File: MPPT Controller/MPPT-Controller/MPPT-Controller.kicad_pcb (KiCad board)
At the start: 4 copper layers, 81 parts, among them J1 Conn_01x02_Pin, J2 Conn_01x02_Pin, J3 Conn_01x02_Pin, J4 Conn_01x02_Pin, J5 USB_C_Receptacle_USB2.0_16P, J6 Conn_01x02_Pin, M1 Fan_4pin, Q1 IRL540N, SW1 SW_SPDT, U1 ADS1115IDGS, U2 ESP32-WROOM-32D, U3 CH340C, U4 LM1117DT-3.3, U5 LM2596S-ADJ, U6 TC4422, U7 ADS1115IDGS

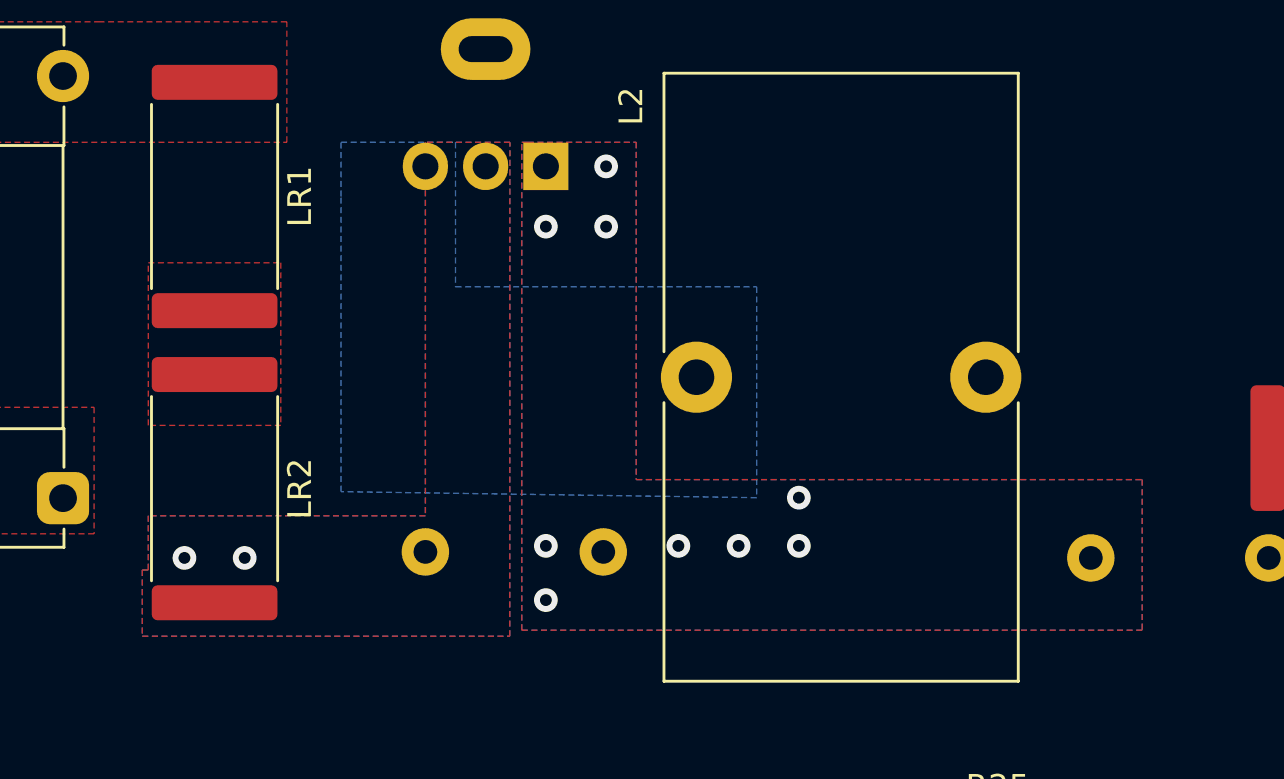
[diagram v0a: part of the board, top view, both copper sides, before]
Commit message: Single Layer
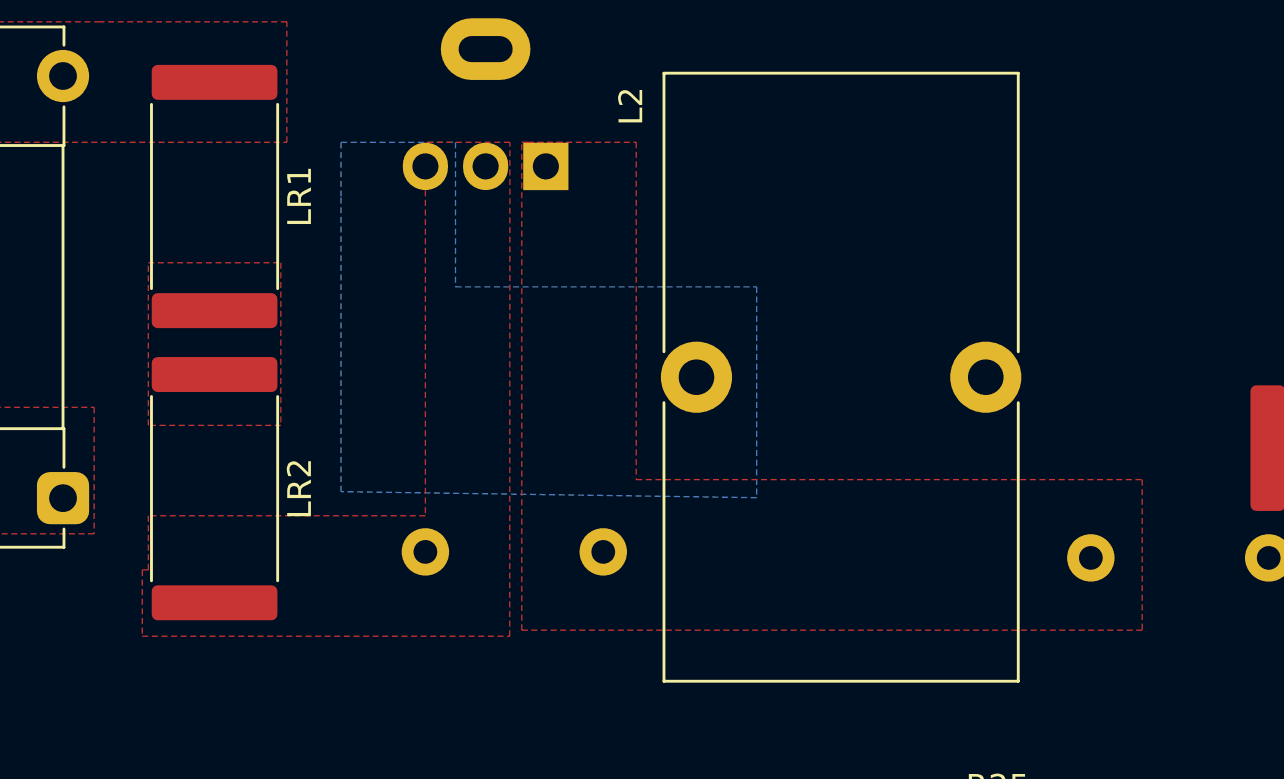
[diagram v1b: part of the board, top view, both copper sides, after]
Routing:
- net VinterA: vias 2 -> 0
- net Net-(D10-A): vias 9 -> 0
- removed copper zone on B.Cu, net Net-(D10-A)
- removed copper zone on B.Cu, net VinterA
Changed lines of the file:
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@@
 		)
 		(property "Value" "470u"
-			(at 3.25 -2 -180)
+			(at 3.25 -2 180)
 			(layer "F.Fab")
 			(effects
@@
 	)
 	(via
-		(at 58.42 121.92)
-		(size 1)
-		(drill 0.5)
-		(layers "F.Cu" "B.Cu")
-		(free yes)
-		(net 4)
-	)
-	(via
-		(at 55.88 121.92)
-		(size 1)
-		(drill 0.5)
-		(layers "F.Cu" "B.Cu")
-		(free yes)
-		(net 4)
-	)
-	(via
 		(at 144 50.5)
 		(size 1)
@@
 		(layers "F.Cu" "B.Cu")
 		(net 13)
-	)
-	(via
-		(at 71.12 107.95)
-		(size 1)
-		(drill 0.5)
-		(layers "F.Cu" "B.Cu")
-		(free yes)
-		(net 15)
-	)
-	(via
-		(at 73.66 107.95)
-		(size 1)
-		(drill 0.5)
-		(layers "F.Cu" "B.Cu")
-		(free yes)
-		(net 15)
-	)
-	(via
-		(at 71.12 123.698)
-		(size 1)
-		(drill 0.5)
-		(layers "F.Cu" "B.Cu")
-		(free yes)
-		(net 15)
-	)
-	(via
-		(at 73.66 105.41)
-		(size 1)
-		(drill 0.5)
-		(layers "F.Cu" "B.Cu")
-		(free yes)
-		(net 15)
-	)
-	(via
-		(at 81.788 119.38)
-		(size 1)
-		(drill 0.5)
-		(layers "F.Cu" "B.Cu")
-		(free yes)
-		(net 15)
-	)
-	(via
-		(at 79.248 121.412)
-		(size 1)
-		(drill 0.5)
-		(layers "F.Cu" "B.Cu")
-		(free yes)
-		(net 15)
-	)
-	(via
-		(at 81.788 121.412)
-		(size 1)
-		(drill 0.5)
-		(layers "F.Cu" "B.Cu")
-		(free yes)
-		(net 15)
-	)
-	(via
-		(at 71.12 121.412)
-		(size 1)
-		(drill 0.5)
-		(layers "F.Cu" "B.Cu")
-		(free yes)
-		(net 15)
-	)
-	(via
-		(at 76.708 121.412)
-		(size 1)
-		(drill 0.5)
-		(layers "F.Cu" "B.Cu")
-		(free yes)
-		(net 15)
 	)
 	(zone
@@
 	)
 	(zone
+		(net 4)
+		(net_name "VinterA")
+		(layer "F.Cu")
+		(hatch edge 0.5)
+		(priority 7)
+		(connect_pads yes
+			(clearance 0.6)
+		)
+		(min_thickness 0.25)
+		(filled_areas_thickness no)
+		(fill yes
+			(thermal_gap 0)
+			(thermal_bridge_width 1)
+		)
+		(polygon
+			(pts
+				(xy 54.356 122.428) (xy 54.102 122.428) (xy 54.102 125.222) (xy 69.596306 125.222) (xy 69.604659 104.394)
+				(xy 66.04 104.394) (xy 66.04 120.142) (xy 54.356 120.142)
+			)
+		)
+	)
+	(zone
 		(net 90)
 		(net_name "Net-(J1-Pin_2)")
@@
 			(pts
 				(xy 30.48 115.57) (xy 52.07 115.57) (xy 52.07 120.904) (xy 30.48 120.904)
+			)
+		)
+	)
+	(zone
+		(net 15)
+		(net_name "Net-(D10-A)")
+		(layer "F.Cu")
+		(hatch edge 0.5)
+		(priority 8)
+		(connect_pads yes
+			(clearance 0.5)
+		)
+		(min_thickness 0.25)
+		(filled_areas_thickness no)
+		(fill yes
+			(thermal_gap 0)
+			(thermal_bridge_width 1)
+		)
+		(polygon
+			(pts
+				(xy 70.358 104.394) (xy 74.93 104.394) (xy 74.93 118.618) (xy 96.266 118.618) (xy 96.266 124.968)
+				(xy 70.104 124.968) (xy 70.104 104.394)
 			)
 		)
@@
 	)
 	(zone
-		(net 4)
-		(net_name "VinterA")
-		(layers "F.Cu" "B.Cu")
-		(hatch edge 0.5)
-		(priority 7)
-		(connect_pads yes
-			(clearance 0.6)
-		)
-		(min_thickness 0.25)
-		(filled_areas_thickness no)
-		(fill yes
-			(thermal_gap 0)
-			(thermal_bridge_width 1)
-		)
-		(polygon
-			(pts
-				(xy 54.356 122.428) (xy 54.102 122.428) (xy 54.102 125.222) (xy 69.596306 125.222) (xy 69.604659 104.394)
-				(xy 66.04 104.394) (xy 66.04 120.142) (xy 54.356 120.142) (xy 54.356 122.428)
-			)
-		)
-	)
-	(zone
 		(net 10)
 		(net_name "+5V")
@@
 	)
 	(zone
-		(net 15)
-		(net_name "Net-(D10-A)")
-		(layers "F.Cu" "B.Cu")
-		(hatch edge 0.5)
-		(priority 8)
-		(connect_pads yes
-			(clearance 0.5)
-		)
-		(min_thickness 0.25)
-		(filled_areas_thickness no)
-		(fill yes
-			(thermal_gap 0)
-			(thermal_bridge_width 1)
-		)
-		(polygon
-			(pts
-				(xy 70.358 104.394) (xy 74.93 104.394) (xy 74.93 118.618) (xy 96.266 118.618) (xy 96.266 124.968)
-				(xy 70.104 124.968) (xy 70.104 104.394)
-			)
-		)
-	)
-	(zone
 		(net 2)
 		(net_name "GND")
@@
 			)
 		)
+	)
+	(zone
+		(net 0)
+		(net_name "")
+		(layer "F.Mask")
+		(hatch edge 0.5)
+		(priority 8)
+		(connect_pads yes
+			(clearance 0.5)
+		)
+		(min_thickness 0.25)
+		(filled_areas_thickness no)
+		(fill yes
+			(thermal_gap 0)
+			(thermal_bridge_width 1)
+		)
+		(polygon
+			(pts
+				(xy 70.1 104.4) (xy 74.93 104.4) (xy 74.93 118.62) (xy 96.26 118.62) (xy 96.26 124.97) (xy 70.1 124.97)
+			)
+		)
